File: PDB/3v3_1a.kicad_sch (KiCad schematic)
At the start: 0 parts

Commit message: Add 3v3@1a
unified the batery lables between sub schematics and changed Iout symbols for power pins to avoid layout issues for trying to match multiple bateries and Iouts without footprints
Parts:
- added Cin: 4.7 uF, symbol Device:C
- added Cout: 22uF, symbol Device:C
- added L1: 1uH, symbol Device:L
- added Rfbb: 100kOhm, symbol Device:R
- added Rfbt: 453kOhm, symbol Device:R
- added U3: TLV62569ADRLR, DRL0006A, symbol sym&foot:TLV62569ADRLR
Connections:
- new net: Rfbb.1, Rfbt.2, U3.1 (FB)
- new net: L1.1, U3.4 (SW)
- new net +3.3V@1A: Cout.1, L1.2, Rfbt.1
- new net +BATT: Cin.1, U3.3 (VIN), U3.5 (EN)
- new net GND: Cin.2, Cout.2, Rfbb.2, U3.2 (GND)
- no-connect marks 0 -> 1

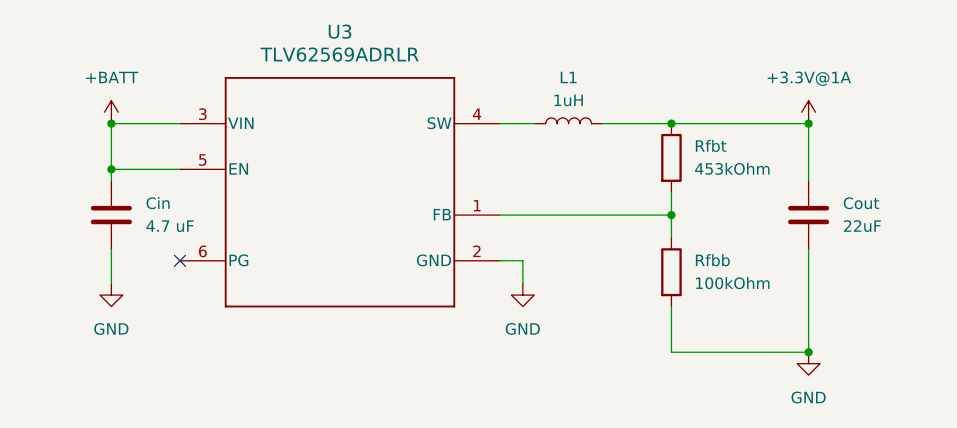
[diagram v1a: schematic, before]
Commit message: Add 24V@1.5A
Filled 24V@1.5A schem and added hierarchal pins to each sub sheet
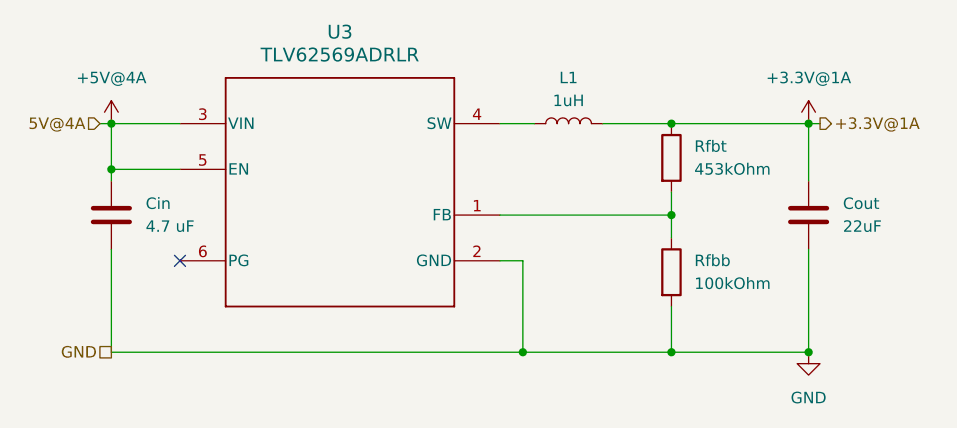
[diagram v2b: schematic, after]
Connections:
- net +BATT renamed +5V@4A
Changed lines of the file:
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@@
+	)
+	(junction
+		(at 149.86 88.9)
+		(diameter 0)
+		(color 0 0 0 0)
 	)
 	(junction
@@
 	)
 	(junction
+		(at 166.37 88.9)
+		(diameter 0)
+		(color 0 0 0 0)
+	)
+	(junction
 		(at 166.37 63.5)
 		(diameter 0)
@@
 	(wire
 		(pts
-			(xy 104.14 77.47) (xy 104.14 81.28)
-		)
-		(stroke
-			(width 0)
-			(type default)
-		)
-	)
-	(wire
-		(pts
 			(xy 147.32 63.5) (xy 151.13 63.5)
 		)
@@
 	(wire
 		(pts
-			(xy 149.86 78.74) (xy 149.86 81.28)
+			(xy 104.14 88.9) (xy 166.37 88.9)
+		)
+		(stroke
+			(width 0)
+			(type default)
+		)
+	)
+	(wire
+		(pts
+			(xy 149.86 78.74) (xy 149.86 88.9)
+		)
+		(stroke
+			(width 0)
+			(type default)
+		)
+	)
+	(wire
+		(pts
+			(xy 102.87 63.5) (xy 104.14 63.5)
 		)
 		(stroke
@@
 	(wire
 		(pts
+			(xy 104.14 77.47) (xy 104.14 88.9)
+		)
+		(stroke
+			(width 0)
+			(type default)
+		)
+	)
+	(wire
+		(pts
 			(xy 166.37 73.66) (xy 166.37 76.2)
 		)
@@
 	(wire
 		(pts
+			(xy 181.61 63.5) (xy 182.88 63.5)
+		)
+		(stroke
+			(width 0)
+			(type default)
+		)
+	)
+	(wire
+		(pts
 			(xy 104.14 63.5) (xy 104.14 68.58)
 		)
@@
 			(width 0)
 			(type default)
+		)
+	)
+	(hierarchical_label "GND"
+		(shape passive)
+		(at 104.14 88.9 180)
+		(effects
+			(font
+				(size 1.27 1.27)
+			)
+			(justify right)
+		)
+	)
+	(hierarchical_label "+3.3V@1A"
+		(shape output)
+		(at 182.88 63.5 0)
+		(effects
+			(font
+				(size 1.27 1.27)
+			)
+			(justify left)
+		)
+	)
+	(hierarchical_label "5V@4A"
+		(shape input)
+		(at 102.87 63.5 180)
+		(effects
+			(font
+				(size 1.27 1.27)
+			)
+			(justify right)
 		)
 	)
@@
 			)
 		)
-		(property "Value" "+BATT"
+		(property "Value" "+5V@4A"
 			(at 104.14 58.42 0)
 			(show_name no)
@@
 	)
 	(symbol
-		(lib_id "power:GND")
-		(at 149.86 81.28 0)
-		(unit 1)
-		(body_style 1)
-		(exclude_from_sim no)
-		(in_bom yes)
-		(on_board yes)
-		(in_pos_files yes)
-		(dnp no)
-		(fields_autoplaced yes)
-		(property "Reference" "#PWR04"
-			(at 149.86 87.63 0)
-			(hide yes)
-			(show_name no)
-			(do_not_autoplace no)
-			(effects
-				(font
-					(size 1.27 1.27)
-				)
-			)
-		)
-		(property "Value" "GND"
-			(at 149.86 86.36 0)
-			(show_name no)
-			(do_not_autoplace no)
-			(effects
-				(font
-					(size 1.27 1.27)
-				)
-			)
-		)
-		(property "Footprint" ""
-			(at 149.86 81.28 0)
-			(hide yes)
-			(show_name no)
-			(do_not_autoplace no)
-			(effects
-				(font
-					(size 1.27 1.27)
-				)
-			)
-		)
-		(property "Datasheet" ""
-			(at 149.86 81.28 0)
-			(hide yes)
-			(show_name no)
-			(do_not_autoplace no)
-			(effects
-				(font
-					(size 1.27 1.27)
-				)
-			)
-		)
-		(property "Description" "Power symbol creates a global label with name \"GND\" , ground"
-			(at 149.86 81.28 0)
-			(hide yes)
-			(show_name no)
-			(do_not_autoplace no)
-			(effects
-				(font
-					(size 1.27 1.27)
-				)
-			)
-		)
-		(pin "1"
-		)
-		(instances
-			(project "PDB"
-				(path "/a9cf05c4-aac5-4cf1-b700-1d3045f8dfbd/eaf0840f-875c-44d4-b065-16bc98c2c6be"
-					(reference "#PWR04")
-					(unit 1)
-				)
-			)
-		)
-	)
-	(symbol
 		(lib_id "Device:L")
 		(at 154.94 63.5 90)
@@
 					(unit 1)
 				)
-			)
-		)
-	)
-	(symbol
-		(lib_id "power:GND")
-		(at 104.14 81.28 0)
-		(unit 1)
-		(body_style 1)
-		(exclude_from_sim no)
-		(in_bom yes)
-		(on_board yes)
-		(in_pos_files yes)
-		(dnp no)
-		(fields_autoplaced yes)
-		(property "Reference" "#PWR07"
-			(at 104.14 87.63 0)
-			(hide yes)
-			(show_name no)
-			(do_not_autoplace no)
-			(effects
-				(font
-					(size 1.27 1.27)
-				)
-			)
-		)
-		(property "Value" "GND"
-			(at 104.14 86.36 0)
-			(show_name no)
-			(do_not_autoplace no)
-			(effects
-				(font
-					(size 1.27 1.27)
-				)
-			)
-		)
-		(property "Footprint" ""
-			(at 104.14 81.28 0)
-			(hide yes)
-			(show_name no)
-			(do_not_autoplace no)
-			(effects
-				(font
-					(size 1.27 1.27)
-				)
-			)
-		)
-		(property "Datasheet" ""
-			(at 104.14 81.28 0)
-			(hide yes)
-			(show_name no)
-			(do_not_autoplace no)
-			(effects
-				(font
-					(size 1.27 1.27)
-				)
-			)
-		)
-		(property "Description" "Power symbol creates a global label with name \"GND\" , ground"
-			(at 104.14 81.28 0)
-			(hide yes)
-			(show_name no)
-			(do_not_autoplace no)
-			(effects
-				(font
-					(size 1.27 1.27)
-				)
-			)
-		)
-		(pin "1"
-		)
-		(instances
-			(project "PDB"
-				(path "/a9cf05c4-aac5-4cf1-b700-1d3045f8dfbd/eaf0840f-875c-44d4-b065-16bc98c2c6be"
-					(reference "#PWR07")
-					(unit 1)
-				)

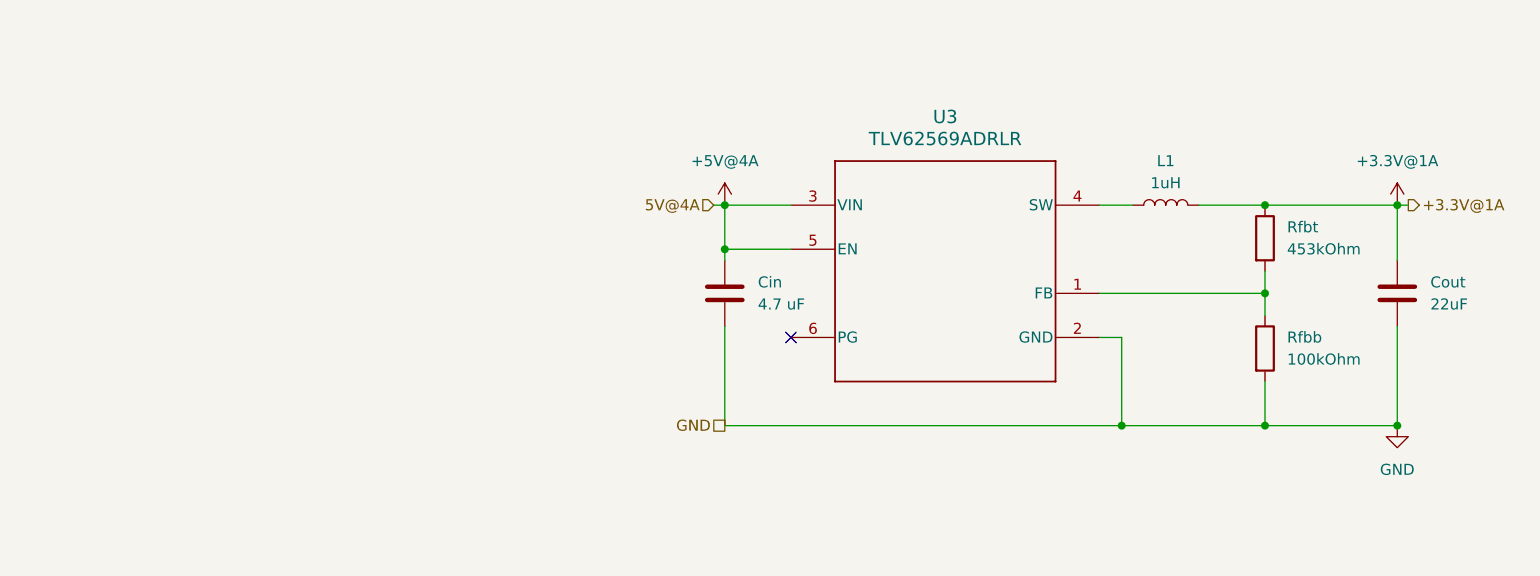
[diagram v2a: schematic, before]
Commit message: added temp sensing on every rail available
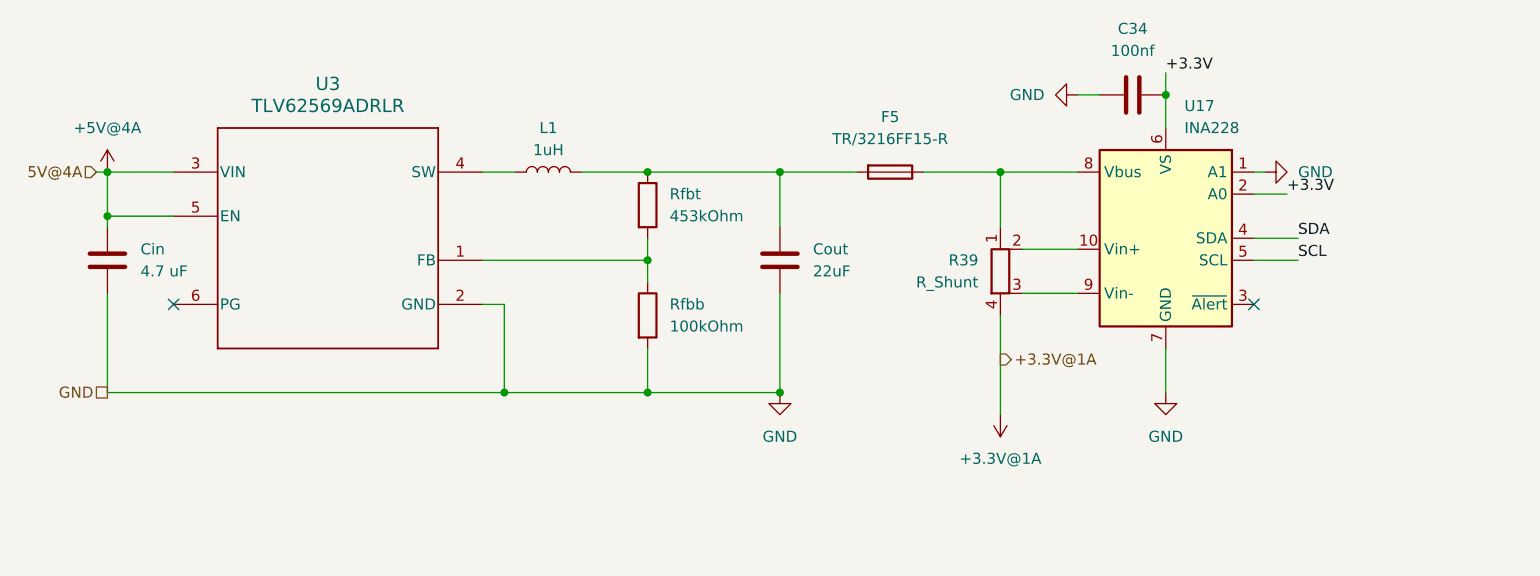
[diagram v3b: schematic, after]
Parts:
- added C34: 100nf, Capacitor_SMD:C_1206_3216Metric, symbol Device:C
- added F5: TR/3216FF15-R, symbol Device:Fuse
- added R39: R_Shunt, symbol Device:R_Shunt
- added U17: INA228, Package_SO:TSSOP-10_3x3mm_P0.5mm, symbol Sensor_Energy:INA228
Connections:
- net +3.3V@1A: now also R39.4; no longer Cout.1, L1.2, Rfbt.1
- net GND: now also C34.1, U17.1 (A1), U17.7 (GND)
- new net: Cout.1, F5.2, L1.2, Rfbt.1
- new net: F5.1, R39.1, U17.8 (Vbus)
- new net: R39.2, U17.10 (Vin+)
- new net: R39.3, U17.9 (Vin-)
- new net +3.3V: C34.2, U17.2 (A0), U17.6 (VS)
- new net SCL: U17.5 (SCL)
- new net SDA: U17.4 (SDA)
- no-connect marks 1 -> 2
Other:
- moved on the sheet: Cin, Cout, L1, Rfbb, Rfbt, U3

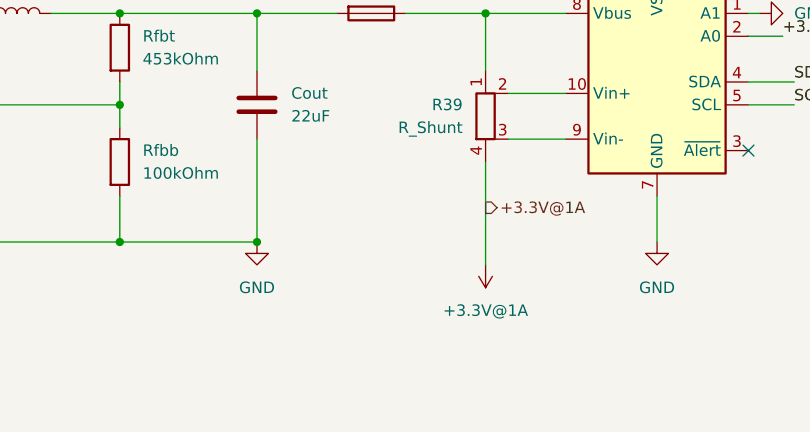
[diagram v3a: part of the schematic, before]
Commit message: added tp's, switches, inputs/outputs
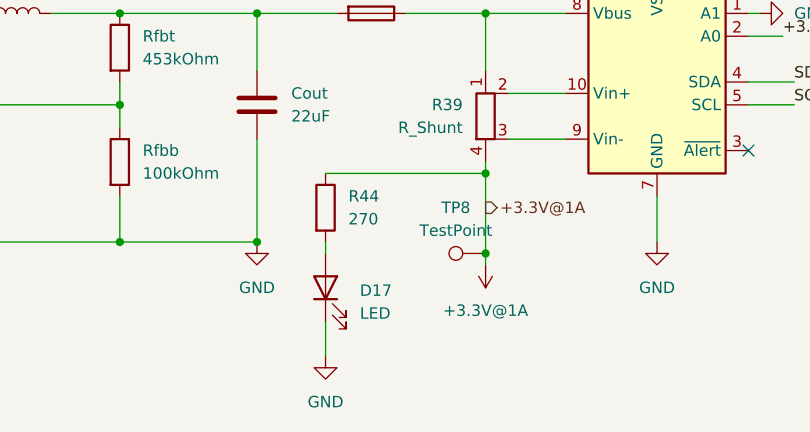
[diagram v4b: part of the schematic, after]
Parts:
- added D17: LED, LED_SMD:LED_0805_2012Metric, symbol Device:LED
- added R44: 270, Resistor_SMD:R_1206_3216Metric_Pad1.30x1.75mm_HandSolder, symbol Device:R
- added TP8: TestPoint, TestPoint:TestPoint_Pad_D2.0mm, symbol Connector:TestPoint
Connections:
- net +3.3V@1A: now also R44.1, TP8.1
- net GND: now also D17.1 (K)
- new net: D17.2 (A), R44.2
